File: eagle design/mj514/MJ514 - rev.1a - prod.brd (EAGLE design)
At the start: 49 x 18 mm, 57 parts, among them IC201 LDK320AM33R, IC203 R3119N058A-TR-FE, IC302 STM32F042G6U6, IC401 TCAN334, IC402 SZNUP2105LT1G, IC501 SHT40-AD1F-R2, IC601 MB85RC16PN-G-AMERE1, IC701 AS5601-ASOM, IC801 LT1935ES5#TRMPBF, IC901 DRV8876RGTR

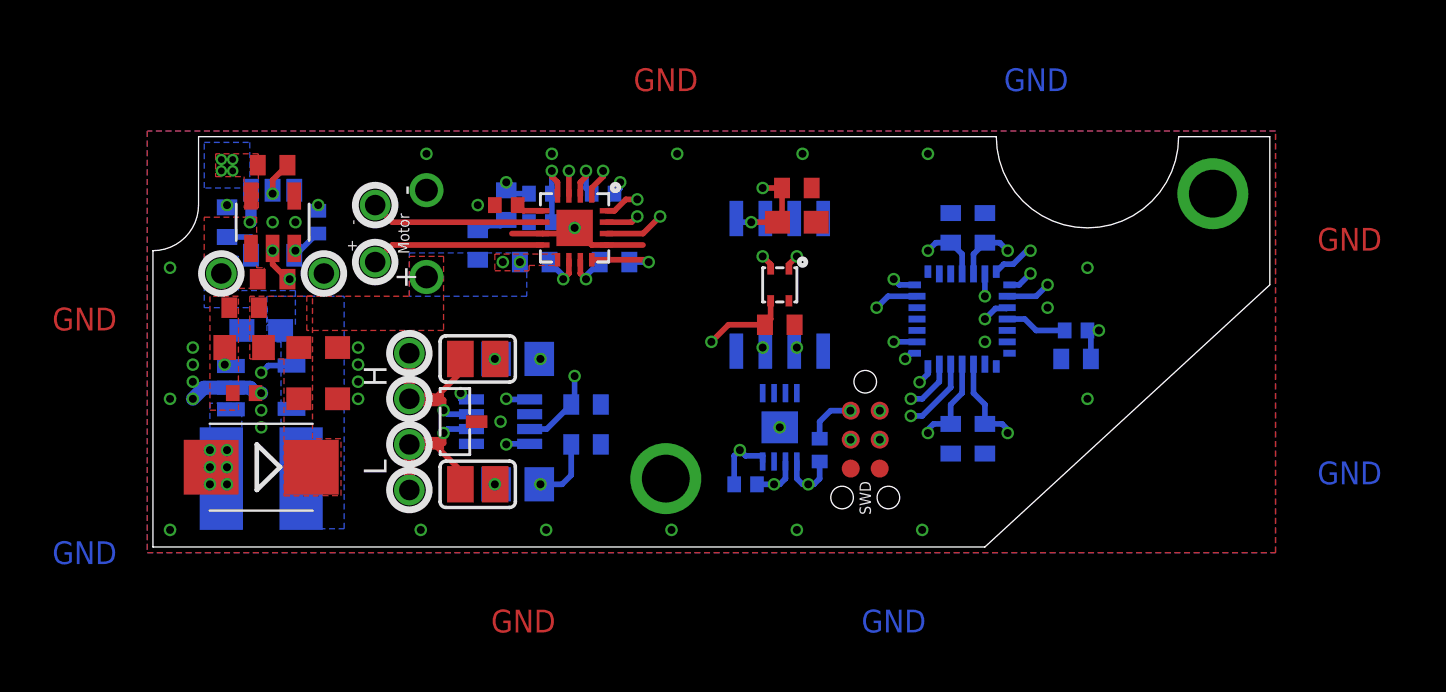
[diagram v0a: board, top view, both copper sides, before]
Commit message: ///////// start of HW Rev.1a ///////// !!! board design is not true hw rev.1a - was manually edited to match actual oshpark fabrication!!!
in mj838.c/.h:
- adapted base hw rev.1 code to hw rev.1a board: moved CAN standby GPIO to PA15

in motor.c/.h:
- manual merge of "raw angles per ms" branch

in board design:
- removed not prod related designs & schematics
- added motor controller Pmode resistor so that oshpark delivered board matches with drawing ( minus 12V0 regulator shutdown line - this still exists in this board)
- moved AS5601 0.5mm east and corrected 3V3 via position
- corrected tplace via markings
- corrected dimensions: N +=0.5mm, E += 1mm
- corrected E screw via hole += 1mm towards N and += 2mm towards E
- rounded a few corners
- in motor controller sheet changed value of Iprop resistor from 1k to 2k2
- added debug0/1/2 GPIOs on PB0/1 & PA7
- moved semi-circular cutout at NE side of board 1mm towards E
- added vias for SWD & 2V2/GND wired connections to programming adapter

board sent to fab
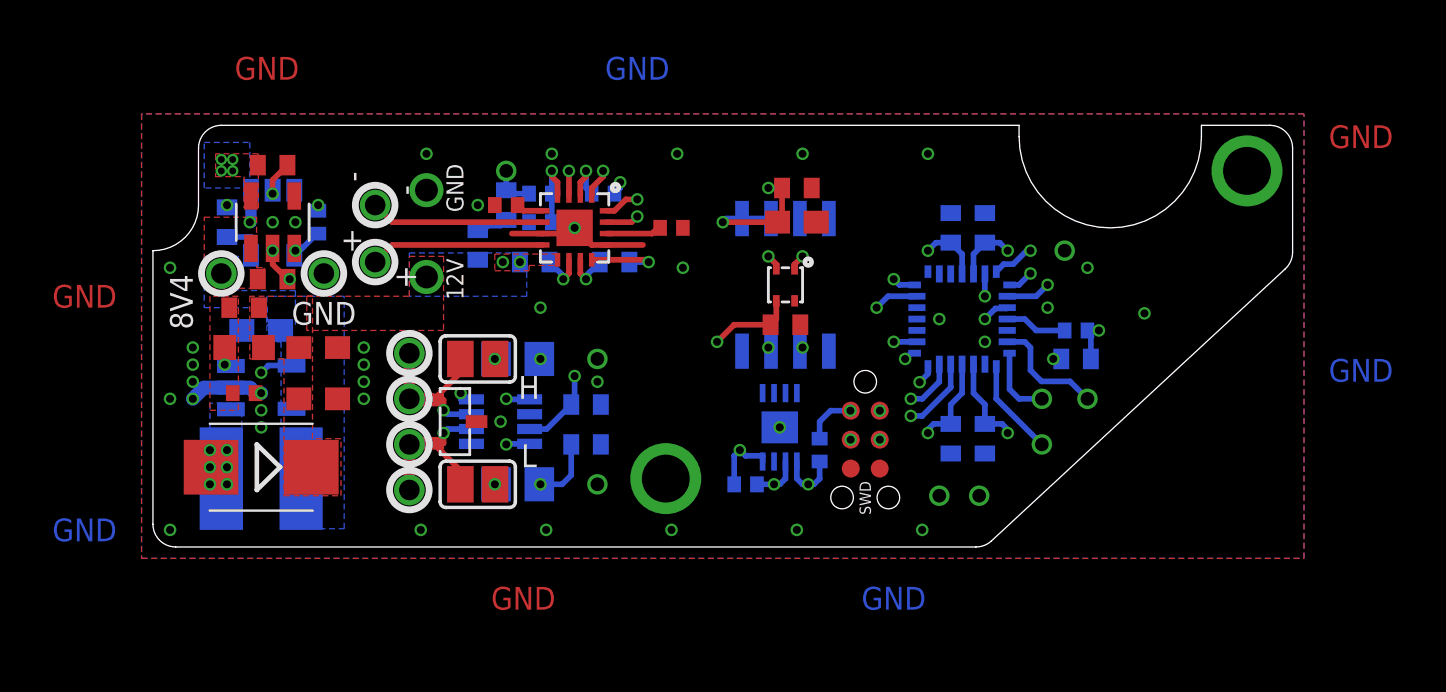
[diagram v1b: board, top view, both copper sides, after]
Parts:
- added 3V3, DEBUG0, DEBUG1, DEBUG2, GND, MOTOR_FLT, MOTOR_IPROP, SWCLK, SWDIO: TP0.6, TP-06:TH
- added R902: foo, rcl:R0402
- R906: value 1k -> 2k2
- moved C501 0.25 mm to (27.8, 9.75)
- moved IC501 0.25 mm to (27.8, 11.5)
- moved IC701 0.25 mm to (27.8, 11.5)
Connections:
- removed net STM32F04:PA7: IC302.13_PA7
- removed net STM32F04:PB0: IC302.14_PB0
- removed net STM32F04:PB1: IC302.15_PB1
- new net DEBUG0: DEBUG0.P$1, IC302.14_PB0
- new net DEBUG1: DEBUG1.P$1, IC302.15_PB1
- new net DEBUG2: DEBUG2.P$1, IC302.13_PA7
- new net MC:PMODE: IC901.P$14, R902.2
- net 3V3: now also 3V3.P$1; no longer IC901.P$14
- net GND: now also GND.P$1, R902.1
- net MOTOR_FLT: now also MOTOR_FLT.P$1
- net MOTOR_IPROP: now also MOTOR_IPROP.P$1
- net SYS_SWCLK: now also SWCLK.P$1
- net SYS_SWDIO: now also SWDIO.P$1
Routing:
- net SYS_SWDIO: track 3.20 -> 9.27 mm
- net DEBUG2: track 0.00 -> 5.14 mm
- net DEBUG1: track 0.00 -> 4.25 mm
- net DEBUG0: track 0.00 -> 3.17 mm
- net MC:PMODE: track 0.00 -> 2.45 mm
- net SYS_SWCLK: track 11.7 -> 12.9 mm
- net MOTOR_FLT: track 28.9 -> 30.0 mm
- net MOTOR_IPROP: track 27.3 -> 28.3 mm, vias 2 -> 1
- net 3V3: track 34.3 -> 33.4 mm, vias 16 -> 15
- net GND: vias 39 -> 44
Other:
- board size 49 x 18 mm -> 50 x 18.5 mm
- board text added: "12V"
- board text added: "8V4"
- board text removed: "Motor"
